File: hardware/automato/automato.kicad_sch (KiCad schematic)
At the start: 25 parts, among them J2 Motor_L, J3 Motor_3, J5 Servo 1, J6 i2c, U1 ESP32-C6-DEVKITC-1-N8, U2 DRV8411APWPR, U3 AP63357DV-7

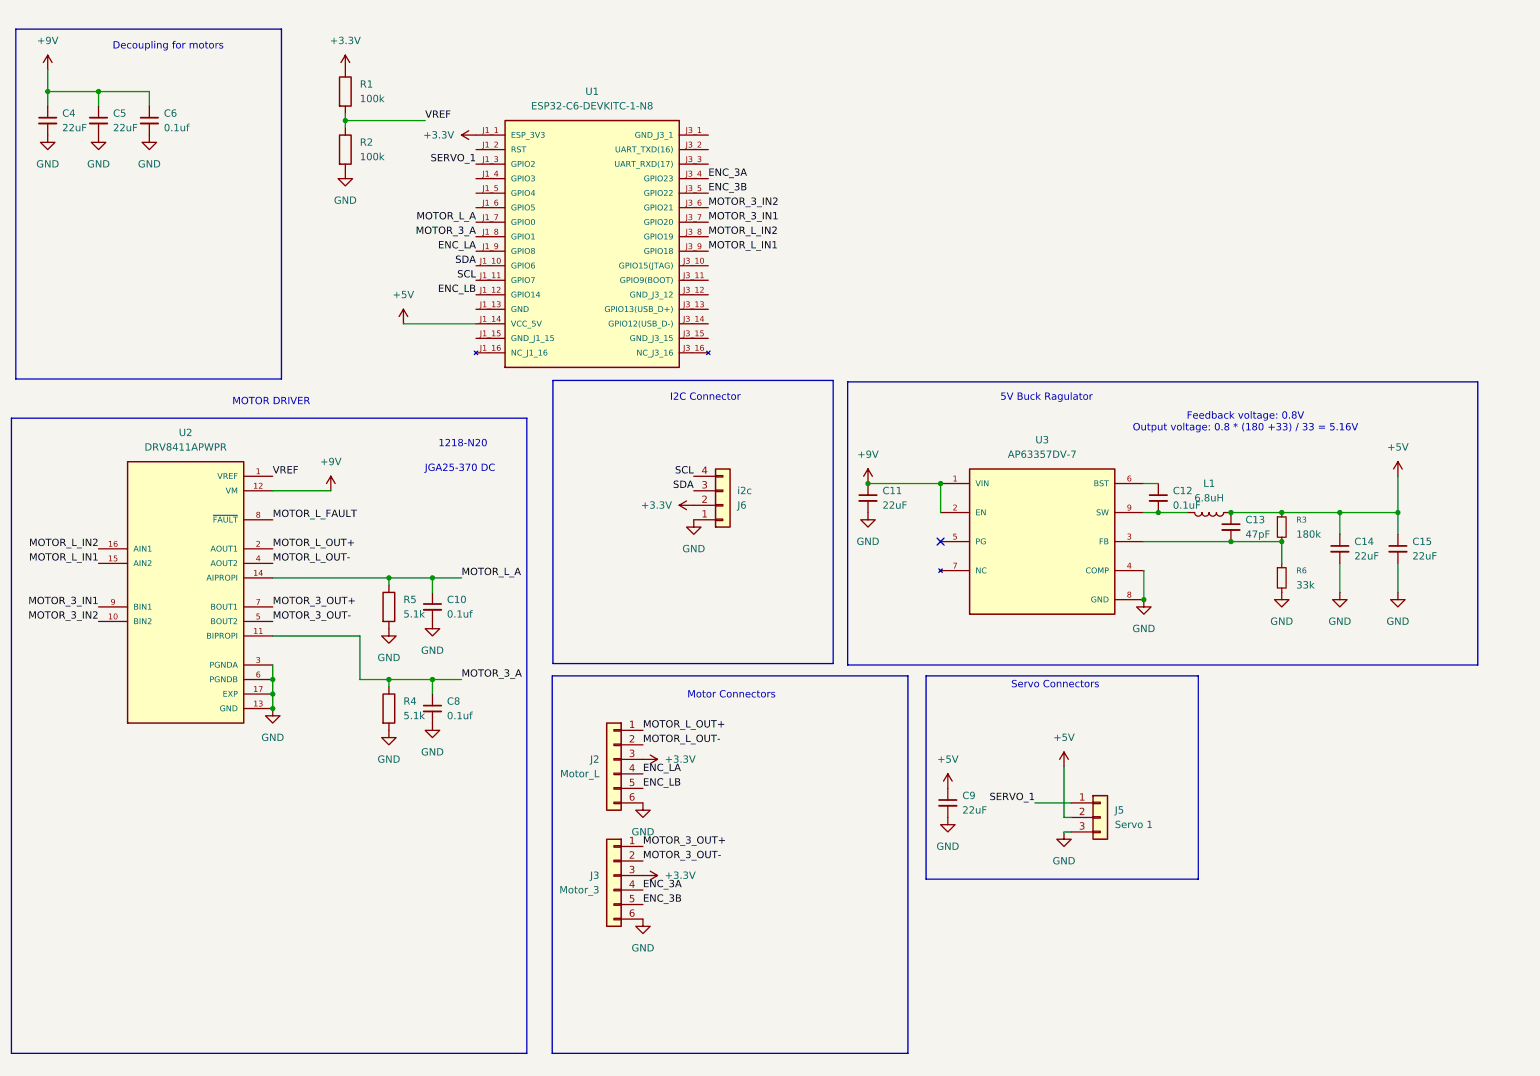
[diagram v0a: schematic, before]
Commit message: added relays and mosfets
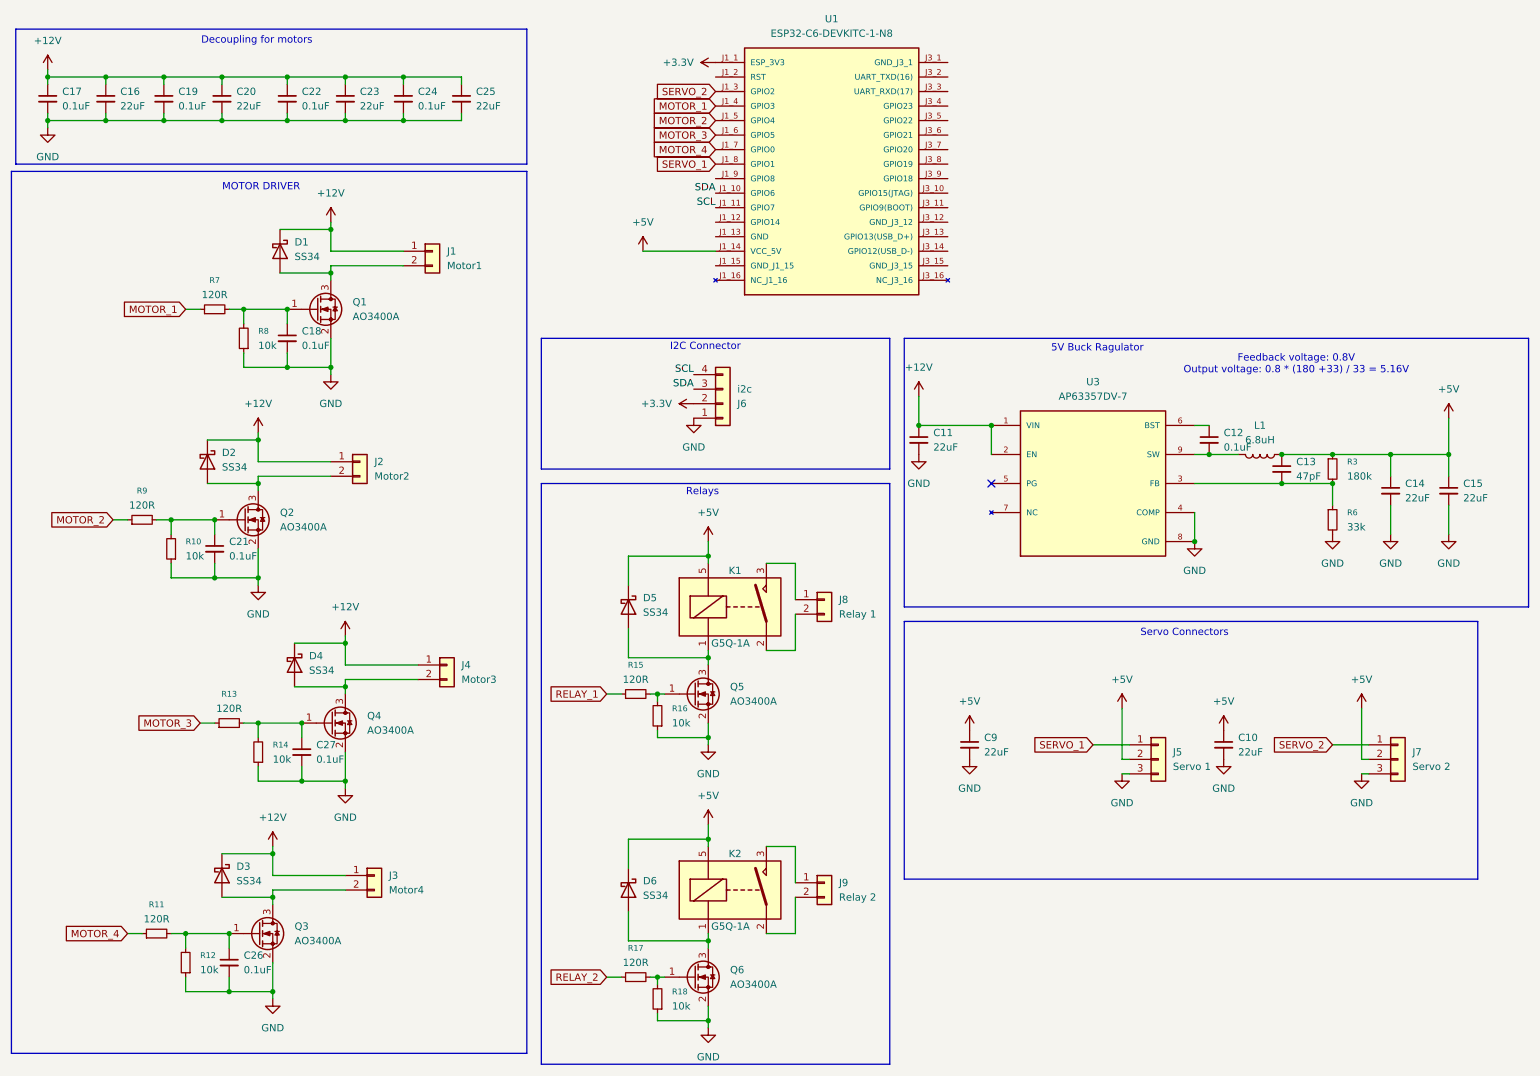
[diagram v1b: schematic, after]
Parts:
- removed C4, C5: 22uF, Capacitor_SMD:C_0805_2012Metric, symbol Device:C_Small
- removed C6, C8: 0.1uf, Capacitor_SMD:C_0603_1608Metric, symbol Device:C_Small
- removed J2: Motor_L, Connector_JST:JST_PH_S6B-PH-K_1x06_P2.00mm_Horizontal, symbol Connector_Generic:Conn_01x06
- removed J3: Motor_3, Connector_JST:JST_PH_S6B-PH-K_1x06_P2.00mm_Horizontal, symbol Connector_Generic:Conn_01x06
- removed R1, R2: 100k, Resistor_SMD:R_0603_1608Metric, symbol Device:R
- removed R4, R5: 5.1k, Resistor_SMD:R_0603_1608Metric, symbol Device:R
- removed U2: DRV8411APWPR, Kjelland:IC_DRV8411APWPR, symbol Kjelland:DRV8411APWPR
- added C16, C20, C23, C25: 22uF, Capacitor_SMD:C_0805_2012Metric, symbol Device:C_Small
- added C17, C18, C19, C21, C22, C24, C26, C27: 0.1uF, Capacitor_SMD:C_0603_1608Metric, symbol Device:C_Small
- added D1, D2, D3, D4, D5, D6: SS34, Diode_SMD:D_SMA, symbol Diode:SS34
- added J1: Motor1, TerminalBlock_Phoenix:TerminalBlock_Phoenix_MKDS-1,5-2-5.08_1x02_P5.08mm_Horizontal, symbol Connector_Generic:Conn_01x02
- added J2: Motor2, TerminalBlock_Phoenix:TerminalBlock_Phoenix_MKDS-1,5-2-5.08_1x02_P5.08mm_Horizontal, symbol Connector_Generic:Conn_01x02
- added J3: Motor4, TerminalBlock_Phoenix:TerminalBlock_Phoenix_MKDS-1,5-2-5.08_1x02_P5.08mm_Horizontal, symbol Connector_Generic:Conn_01x02
- added J4: Motor3, TerminalBlock_Phoenix:TerminalBlock_Phoenix_MKDS-1,5-2-5.08_1x02_P5.08mm_Horizontal, symbol Connector_Generic:Conn_01x02
- added J7: Servo 2, Connector_PinHeader_2.54mm:PinHeader_1x03_P2.54mm_Vertical, symbol Connector_Generic:Conn_01x03
- added J8: Relay 1, TerminalBlock_Phoenix:TerminalBlock_Phoenix_MKDS-1,5-2-5.08_1x02_P5.08mm_Horizontal, symbol Connector_Generic:Conn_01x02
- added J9: Relay 2, TerminalBlock_Phoenix:TerminalBlock_Phoenix_MKDS-1,5-2-5.08_1x02_P5.08mm_Horizontal, symbol Connector_Generic:Conn_01x02
- added K1, K2: G5Q-1A, Relay_THT:Relay_SPST_Omron-G5Q-1A, symbol Relay:G5Q-1A
- added Q1, Q2, Q3, Q4, Q5, Q6: AO3400A, Package_TO_SOT_SMD:SOT-23, symbol Transistor_FET:AO3400A
- added R10, R12, R14, R16, R18, R8: 10k, Resistor_SMD:R_0603_1608Metric, symbol Device:R_Small
- added R11, R13, R15, R17, R7, R9: 120R, Resistor_SMD:R_0603_1608Metric, symbol Device:R_Small
- C10: value 0.1uf -> 22uF; footprint Capacitor_SMD:C_0603_1608Metric -> Capacitor_SMD:C_0805_2012Metric
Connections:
- net MOTOR_3_A is gone; now on net SERVO_1: U1.J1_8 (GPIO1)
- net +5V: now also C10.1, D5.1 (K), D6.1 (K), J7.2 (Pin_2), K1.5, K2.5
- net GND: now also C16.2, C17.2, C18.2, C19.2, C20.2, C21.2, C22.2, C23.2, C24.2, C25.2, C26.2, C27.2, J7.3 (Pin_3), Q1.2 (S), Q2.2 (S), Q3.2 (S), Q4.2 (S), Q5.2 (S), Q6.2 (S), R10.1, R12.1, R14.1, R16.1, R18.1, R8.1
- net SERVO_1: no longer U1.J1_3 (GPIO2)
- net MOTOR_1: now reaches U1.J1_4 (GPIO3)
- net MOTOR_1: now also R7.1
- net MOTOR_2: now reaches U1.J1_5 (GPIO4)
- net MOTOR_2: now also R9.1
- net MOTOR_3: now reaches U1.J1_6 (GPIO5)
- net MOTOR_3: now also R13.1
- net +9V renamed +12V
- net +12V: now also C16.1, C17.1, C19.1, C20.1, C22.1, C23.1, C24.1, C25.1, D1.1 (K), D2.1 (K), D3.1 (K), D4.1 (K), J1.1 (Pin_1), J2.1 (Pin_1), J3.1 (Pin_1), J4.1 (Pin_1)
- net ENC_3A: no longer names the net of U1.J3_4 (GPIO23)
- net ENC_3B: no longer names the net of U1.J3_5 (GPIO22)
- net ENC_LA: no longer names the net of U1.J1_9 (GPIO8)
- net ENC_LB: no longer names the net of U1.J1_12 (GPIO14)
- net MOTOR_3_IN1: no longer names the net of U1.J3_7 (GPIO20)
- net MOTOR_3_IN2: no longer names the net of U1.J3_6 (GPIO21)
- net MOTOR_L_A renamed MOTOR_4
- net MOTOR_4: now also R11.1; no longer C10.1
- net MOTOR_L_IN1: no longer names the net of U1.J3_9 (GPIO18)
- net MOTOR_L_IN2: no longer names the net of U1.J3_8 (GPIO19)
- new net: Q5.1 (G), R15.2, R16.2
- new net: C18.1, Q1.1 (G), R7.2, R8.2
- new net: Q6.1 (G), R17.2, R18.2
- new net: D6.2 (A), K2.1, Q6.3 (D)
- new net: J9.2 (Pin_2), K2.2
- new net: J9.1 (Pin_1), K2.3
- new net: D2.2 (A), J2.2 (Pin_2), Q2.3 (D)
- new net: D4.2 (A), J4.2 (Pin_2), Q4.3 (D)
- new net: C21.1, Q2.1 (G), R10.2, R9.2
- new net: D3.2 (A), J3.2 (Pin_2), Q3.3 (D)
- new net: D1.2 (A), J1.2 (Pin_2), Q1.3 (D)
- new net: C27.1, Q4.1 (G), R13.2, R14.2
- new net: J8.1 (Pin_1), K1.3
- new net: J8.2 (Pin_2), K1.2
- new net: D5.2 (A), K1.1, Q5.3 (D)
- new net: C26.1, Q3.1 (G), R11.2, R12.2
- new net RELAY_1: R15.1
- new net RELAY_2: R17.1
- new net SERVO_2: J7.1 (Pin_1), U1.J1_3 (GPIO2)
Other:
- note added: "Relays"
- note removed: "1218-N20"
- note removed: "JGA25-370 DC"
- note removed: "Motor Connectors"
- moved on the sheet: C11, C12, C13, C14, C15, C9, J5, J6, L1, R3, R6, U1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

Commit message: started layout
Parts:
- added C28, C29: 22uF, Capacitor_SMD:C_0805_2012Metric, symbol Device:C_Small
- added FID1, FID2, FID3, FID4: Fiducial, Fiducial:Fiducial_1.5mm_Mask3mm, symbol Mechanical:Fiducial
- added H1, H2, H3, H4: MountingHole, MountingHole:MountingHole_3.2mm_M3, symbol Mechanical:MountingHole
- added J10: Servo 3, Connector_PinHeader_2.54mm:PinHeader_1x03_P2.54mm_Vertical, symbol Connector_Generic:Conn_01x03
- added J11: Servo 4, Connector_PinHeader_2.54mm:PinHeader_1x03_P2.54mm_Vertical, symbol Connector_Generic:Conn_01x03
- added J12: Barrel_Jack, Connector_BarrelJack:BarrelJack_Horizontal, symbol Connector:Barrel_Jack
- added R19, R20: 4.7k, Resistor_SMD:R_0603_1608Metric, symbol Device:R_Small
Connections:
- net +12V: now also J12.1
- net +3.3V: now also R19.2, R20.2
- net +5V: now also C28.1, C29.1, J10.2 (Pin_2), J11.2 (Pin_2)
- net GND: now also U1.J1_13 (GND), U1.J1_15 (GND_J1_15), U1.J3_1 (GND_J3_1), U1.J3_12 (GND_J3_12), U1.J3_15 (GND_J3_15), C28.2, C29.2, J10.3 (Pin_3), J11.3 (Pin_3), J12.2
- net MOTOR_1: now also U1.J3_6 (GPIO21); no longer U1.J1_4 (GPIO3)
- net MOTOR_2: now also U1.J3_7 (GPIO20); no longer U1.J1_5 (GPIO4)
- net MOTOR_3: now also U1.J3_8 (GPIO19); no longer U1.J1_6 (GPIO5)
- net MOTOR_4: now also U1.J3_9 (GPIO18); no longer U1.J1_7 (GPIO0)
- net RELAY_1: now also U1.J1_12 (GPIO14), U1.J1_7 (GPIO0)
- net RELAY_2: now also U1.J1_8 (GPIO1)
- net SCL: now also R19.1
- net SDA: now also R20.1
- net SERVO_1: now also U1.J3_4 (GPIO23); no longer U1.J1_8 (GPIO1)
- net SERVO_2: now also U1.J3_5 (GPIO22); no longer U1.J1_3 (GPIO2)
- new net SERVO_3: J10.1 (Pin_1), U1.J1_3 (GPIO2)
- new net SERVO_4: J11.1 (Pin_1), U1.J1_4 (GPIO3)
- no-connect marks 1 -> 11
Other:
- moved on the sheet: C10, C11, C12, C13, C14, C15, C9, J5, J7, L1, R3, R6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

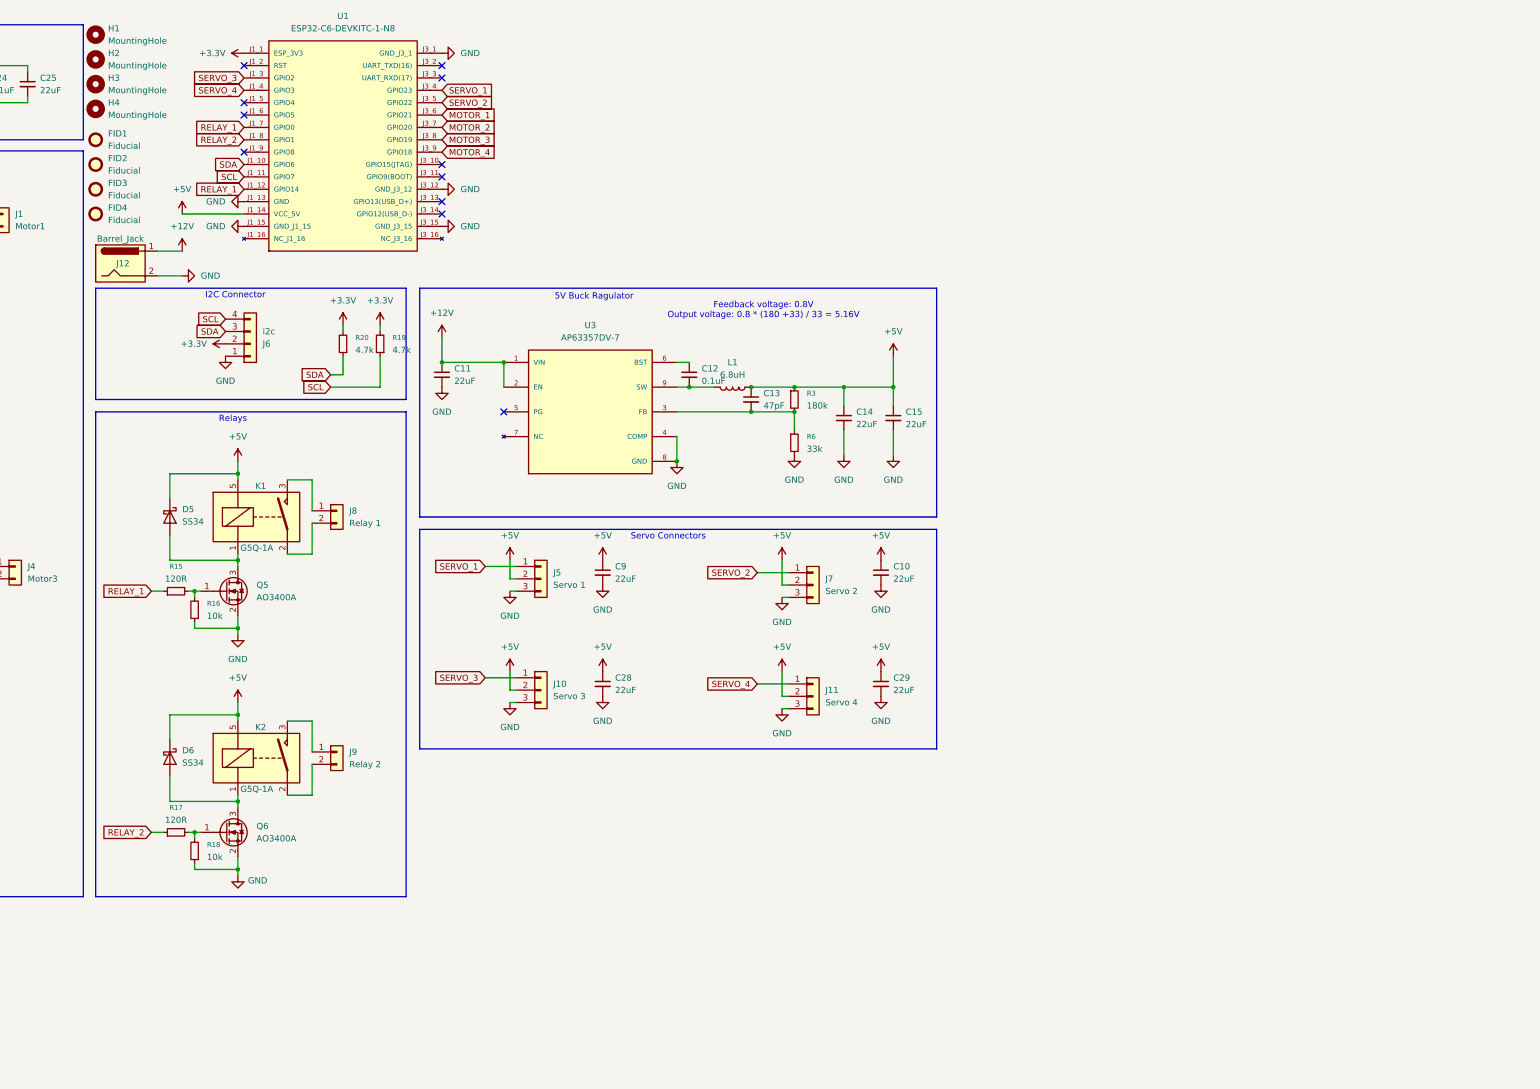
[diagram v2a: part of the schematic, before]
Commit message: changed 5v power supply
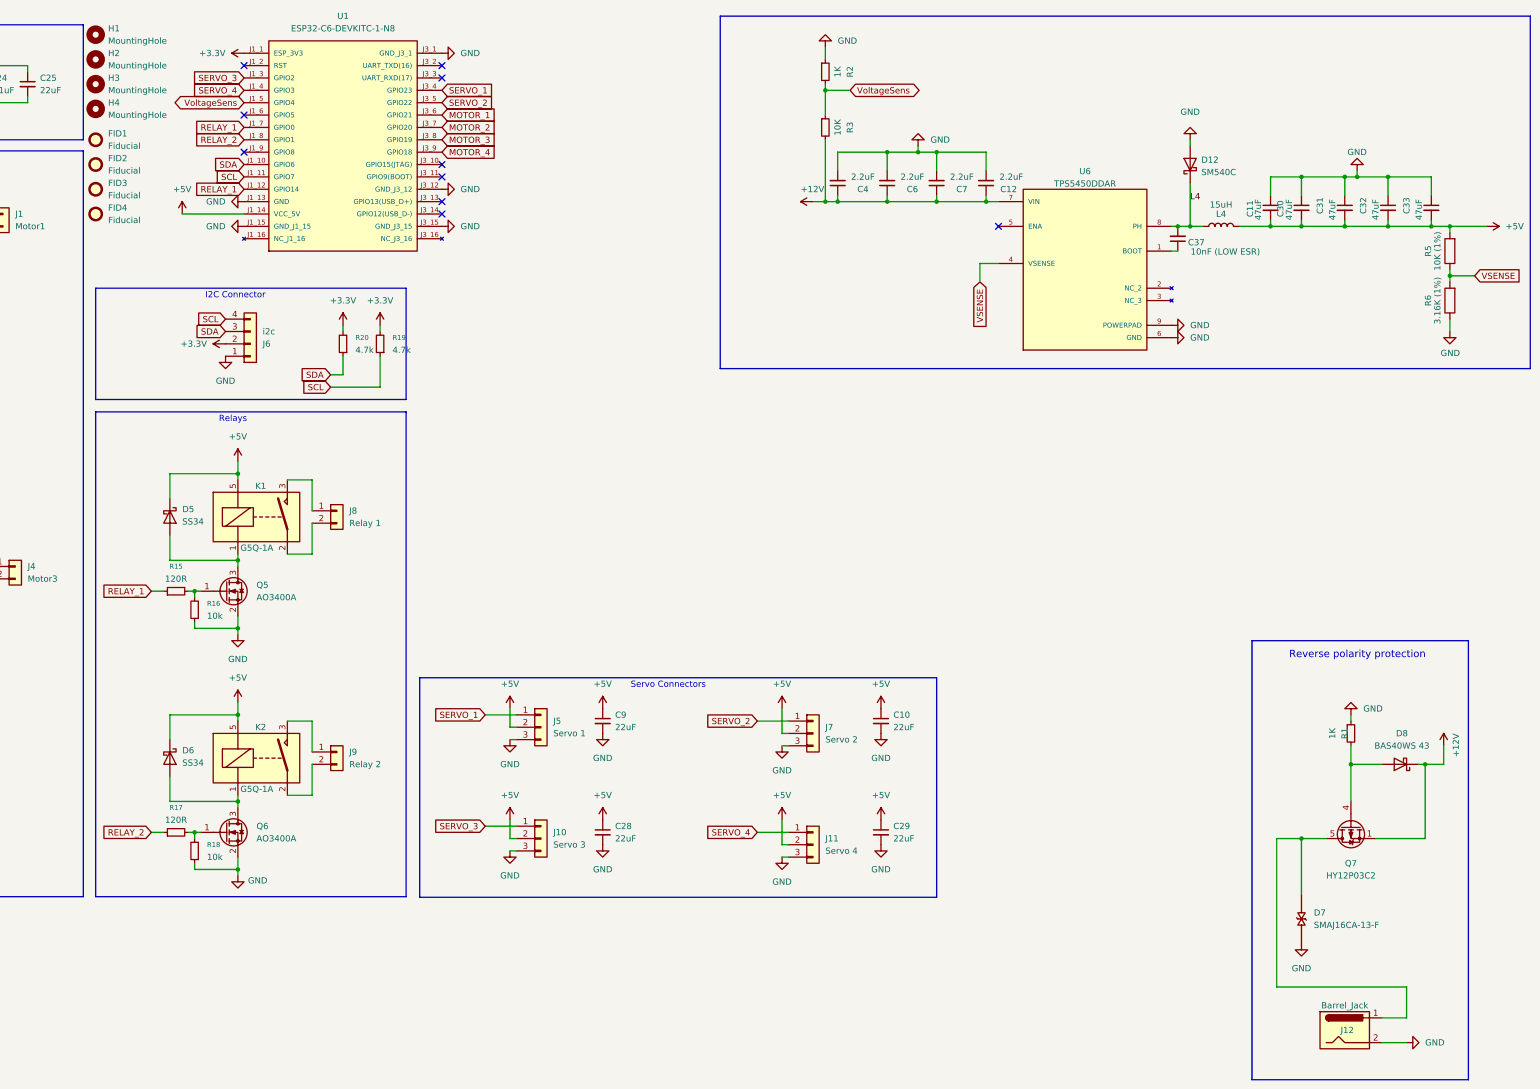
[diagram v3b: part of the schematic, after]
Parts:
- removed C13: 47pF, Capacitor_SMD:C_0603_1608Metric, symbol Device:C_Small
- removed C14, C15: 22uF, Capacitor_SMD:C_0805_2012Metric, symbol Device:C_Small
- removed L1: 6.8uH, Inductor_SMD:L_Wuerth_HCM-1078, symbol Device:L
- removed R6: 33k, Resistor_SMD:R_0603_1608Metric, symbol Device:R_Small
- removed U3: AP63357DV-7, Kjelland:CONV_AP63357DV-7, symbol Kjelland:AP63357DV-7
- added C30, C31, C32, C33: 47uF, Capacitor_SMD:C_0805_2012Metric, symbol Device:C_Small
- added C37: 10nF (LOW ESR), Capacitor_SMD:C_0402_1005Metric, symbol Device:C_Small
- added C4, C6, C7: 2.2uF, Capacitor_SMD:C_0805_2012Metric, symbol Device:C_Small
- added D12: SM540C, Diode_SMD:D_SMC, symbol Device:D_Schottky
- added D7: SMAJ16CA-13-F, BlackPanda:DIOM4325X250N, symbol SMAJ16CA:SMAJ16CA
- added D8: BAS40WS 43, Diode_SMD:D_SOD-323, symbol Device:D_Schottky
- added L4: 15uH, BlackPanda:L_10.5x11.5_H4.0, symbol Device:L
- added Q7: HY12P03C2, Package_SO:PowerPAK_SO-8_Single, symbol Transistor_FET:Si7141DP
- added R1, R2: 1K, Resistor_SMD:R_0402_1005Metric, symbol Device:R_Small
- added R5: 10K (1%), Resistor_SMD:R_0402_1005Metric, symbol Device:R
- added R6: 3.16K (1%), Capacitor_SMD:C_0603_1608Metric, symbol Device:R
- added U6: TPS5450DDAR, BlackPanda:CONV_TPS5450DDAR, symbol TPS5450DDAR:TPS5450DDAR
- C11: value 22uF -> 47uF; Note (none) -> 100V Ceramic X5R
- C12: value 0.1uF -> 2.2uF; footprint Capacitor_SMD:C_0603_1608Metric -> Capacitor_SMD:C_0805_2012Metric
- R3: value 180k -> 10K; footprint Resistor_SMD:R_0603_1608Metric -> Resistor_SMD:R_0402_1005Metric
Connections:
- net +12V: now also C12.1, R3.2, C4.1, C6.1, C7.1, D8.1 (K), Q7.1 (S), Q7.2 (S), Q7.3 (S), U6.7 (VIN); no longer C11.1, J12.1
- net +5V: now also C11.2, C30.2, C31.2, C32.2, C33.2, L4.2, R5.2; no longer R3.1
- net GND: now also C11.1, C12.2, C30.1, C31.1, C32.1, C33.1, C4.2, C6.2, C7.2, D12.2 (A), D7.1, R1.1, R2.1, R6.1, U6.6 (GND), U6.9 (POWERPAD); no longer C11.2
- net VoltageSens: now reaches U1.J1_5 (GPIO4)
- net VoltageSens: now also R3.1, R2.2
- new net: C37.1, U6.1 (BOOT)
- new net: D7.2, J12.1, Q7.5 (D)
- new net: D8.2 (A), Q7.4 (G), R1.2
- new net L4: C37.2, D12.1 (K), L4.1, U6.8 (PH)
- new net VSENSE: R5.1, R6.2, U6.4 (VSENSE)
- no-connect marks 11 -> 10
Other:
- note added: "Reverse polarity protection"
- note removed: "5V Buck Ragulator"
- note removed: "Feedback voltage: 0.8V Output voltage: 0.8 * (180 +33) / 33 = 5.16V"
- moved on the sheet: C10, C28, C29, C9, J10, J11, J5, J7
